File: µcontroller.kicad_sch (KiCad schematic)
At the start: 15 parts, among them U1 stm32G4

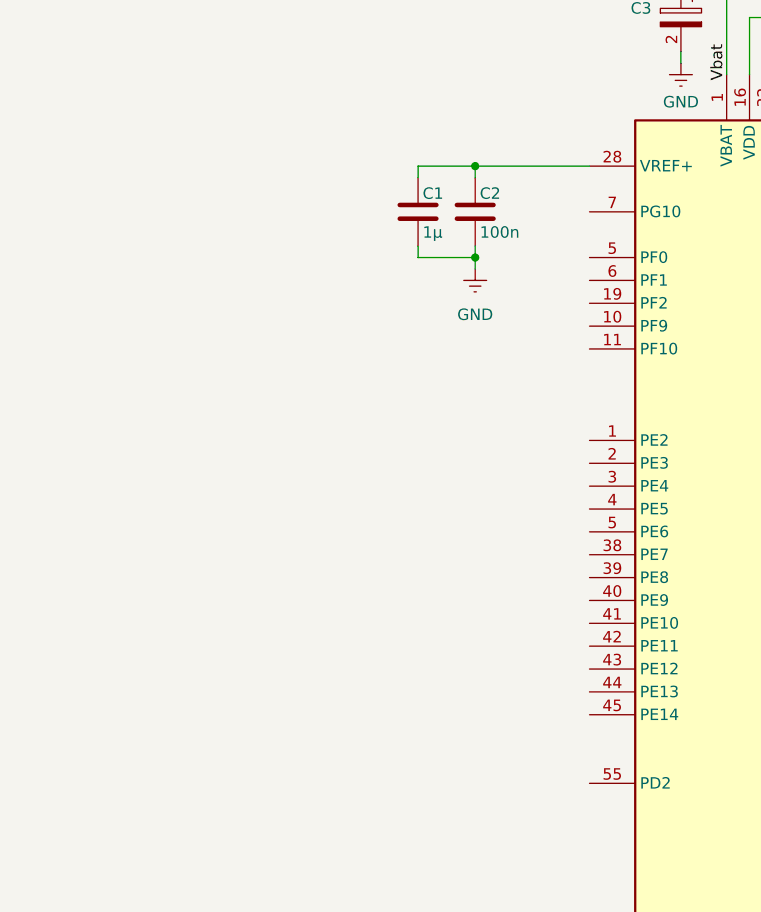
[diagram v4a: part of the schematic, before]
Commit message: pcb gesorteerd
al de main blokken bij elkaar gezet
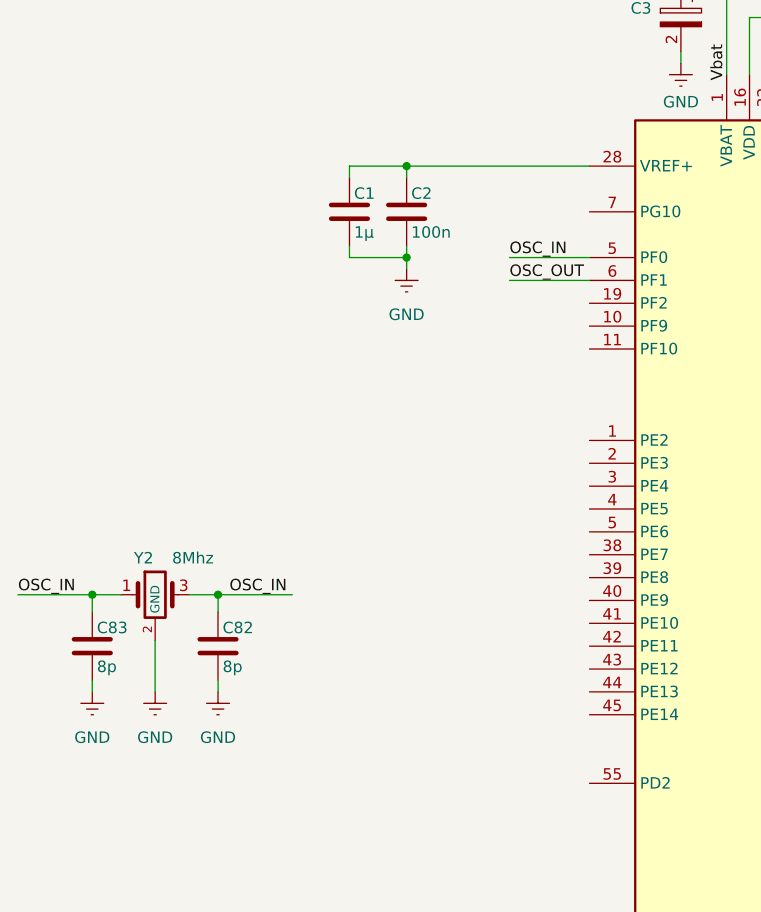
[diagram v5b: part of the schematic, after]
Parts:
- added C82, C83: 8p, Capacitor_SMD:C_0603_1608Metric, symbol Device:C
- added Y2: 8Mhz, Footprintsymbolen_samen:25Mhz crystal 8pF, symbol Schemasymbolen_samen:25Mhz_crystal
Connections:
- net GND: now also C82.2, C83.2, Y2.2 (GND)
- net OSC_IN: now reaches U1.5 (PE6)
- net OSC_IN: now also C82.1, C83.1, Y2.1, Y2.3
- net OSC_OUT: now reaches U1.6 (PF1)
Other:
- moved on the sheet: C1, C2

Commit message: al de main blokken bij elkaar gezet op juiste plaats
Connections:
- net GND: now also Y2.4 (GND)
- net OSC_IN: no longer C82.1, Y2.3
- net OSC_OUT: now also C82.1, Y2.3
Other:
- moved on the sheet: C82, C83, Y2
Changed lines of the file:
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@@
 	)
 	(junction
-		(at 67.945 99.695)
+		(at 68.58 100.33)
 		(diameter 0)
 		(color 0 0 0 0)
@@
 	)
 	(junction
-		(at 53.975 99.695)
+		(at 53.34 100.33)
 		(diameter 0)
 		(color 0 0 0 0)
@@
 	(wire
 		(pts
-			(xy 64.77 99.695) (xy 67.945 99.695)
+			(xy 64.77 100.33) (xy 77.47 100.33)
 		)
 		(stroke
@@
 	(wire
 		(pts
-			(xy 53.975 99.695) (xy 57.15 99.695)
-		)
-		(stroke
-			(width 0)
-			(type default)
-		)
-	)
-	(wire
-		(pts
 			(xy 154.94 85.09) (xy 158.75 85.09)
 		)
@@
 	(wire
 		(pts
-			(xy 53.975 99.695) (xy 53.975 101.6)
+			(xy 53.34 100.33) (xy 53.34 101.6)
 		)
 		(stroke
@@
 	(wire
 		(pts
+			(xy 60.96 105.41) (xy 60.96 110.49)
+		)
+		(stroke
+			(width 0)
+			(type default)
+		)
+	)
+	(wire
+		(pts
 			(xy 188.595 35.56) (xy 194.945 35.56)
 		)
@@
 	(wire
 		(pts
-			(xy 45.72 99.695) (xy 53.975 99.695)
+			(xy 45.72 100.33) (xy 57.15 100.33)
 		)
 		(stroke
@@
 	(wire
 		(pts
-			(xy 67.945 109.22) (xy 67.945 110.49)
+			(xy 68.58 109.22) (xy 68.58 110.49)
 		)
 		(stroke
@@
 	(wire
 		(pts
-			(xy 67.945 99.695) (xy 67.945 101.6)
+			(xy 68.58 100.33) (xy 68.58 101.6)
 		)
 		(stroke
@@
 	(wire
 		(pts
-			(xy 53.975 109.22) (xy 53.975 110.49)
+			(xy 53.34 109.22) (xy 53.34 110.49)
 		)
 		(stroke
@@
 	(wire
 		(pts
-			(xy 60.96 104.775) (xy 60.96 110.49)
-		)
-		(stroke
-			(width 0)
-			(type default)
-		)
-	)
-	(wire
-		(pts
 			(xy 134.62 186.69) (xy 134.62 189.23)
 		)
@@
 	(wire
 		(pts
-			(xy 67.945 99.695) (xy 76.2 99.695)
-		)
-		(stroke
-			(width 0)
-			(type default)
-		)
-	)
-	(wire
-		(pts
 			(xy 127 35.56) (xy 129.54 35.56)
 		)
@@
 		)
 	)
-	(label "OSC_IN"
-		(at 69.215 99.695 0)
+	(label "OSC_OUT"
+		(at 69.215 100.33 0)
 		(effects
 			(font
@@
 	)
 	(label "OSC_IN"
-		(at 45.72 99.695 0)
+		(at 45.72 100.33 0)
 		(effects
 			(font
@@
 	(symbol
 		(lib_id "Device:C")
-		(at 67.945 105.41 0)
+		(at 68.58 105.41 0)
 		(unit 1)
 		(body_style 1)
@@
 		(dnp no)
 		(property "Reference" "C82"
-			(at 68.453 103.378 0)
+			(at 69.088 103.378 0)
 			(show_name no)
 			(do_not_autoplace no)
@@
 		)
 		(property "Value" "8p"
-			(at 68.453 107.696 0)
+			(at 69.088 107.696 0)
 			(show_name no)
 			(do_not_autoplace no)
@@
 		)
 		(property "Footprint" "Capacitor_SMD:C_0603_1608Metric"
-			(at 68.9102 109.22 0)
+			(at 69.5452 109.22 0)
 			(hide yes)
 			(show_name no)
@@
 		)
 		(property "Datasheet" ""
-			(at 67.945 105.41 0)
+			(at 68.58 105.41 0)
 			(hide yes)
 			(show_name no)
@@
 		)
 		(property "Description" "Unpolarized capacitor"
-			(at 67.945 105.41 0)
+			(at 68.58 105.41 0)
 			(hide yes)
 			(show_name no)
@@
 	(symbol
 		(lib_id "Device:C")
-		(at 53.975 105.41 0)
+		(at 53.34 105.41 0)
 		(unit 1)
 		(body_style 1)
@@
 		(dnp no)
 		(property "Reference" "C83"
-			(at 54.483 103.378 0)
+			(at 53.848 103.378 0)
 			(show_name no)
 			(do_not_autoplace no)
@@
 		)
 		(property "Value" "8p"
-			(at 54.483 107.696 0)
+			(at 53.848 107.696 0)
 			(show_name no)
 			(do_not_autoplace no)
@@
 		)
 		(property "Footprint" "Capacitor_SMD:C_0603_1608Metric"
-			(at 54.9402 109.22 0)
+			(at 54.3052 109.22 0)
 			(hide yes)
 			(show_name no)
@@
 		)
 		(property "Datasheet" ""
-			(at 53.975 105.41 0)
+			(at 53.34 105.41 0)
 			(hide yes)
 			(show_name no)
@@
 		)
 		(property "Description" "Unpolarized capacitor"
-			(at 53.975 105.41 0)
+			(at 53.34 105.41 0)
 			(hide yes)
 			(show_name no)
@@
 	(symbol
 		(lib_id "Schemasymbolen_samen:25Mhz_crystal")
-		(at 57.15 98.425 0)
+		(at 57.15 99.06 0)
 		(unit 1)
 		(body_style 1)
@@
 		(dnp no)
 		(property "Reference" "Y2"
-			(at 59.69 95.631 0)
+			(at 59.69 96.266 0)
 			(show_name no)
 			(do_not_autoplace no)
@@
 		)
 		(property "Value" "8Mhz"
-			(at 65.151 95.631 0)
+			(at 65.151 96.266 0)
 			(show_name no)
 			(do_not_autoplace no)
@@
 		)
 		(property "Footprint" "Footprintsymbolen_samen:25Mhz crystal 8pF"
-			(at 52.578 88.011 0)
+			(at 52.578 88.646 0)
 			(hide yes)
 			(show_name no)
@@
 		)
 		(property "Datasheet" "https://www.mouser.be/datasheet/3/1460/1/LFXTAL085880.pdf"
-			(at 73.152 92.837 0)
+			(at 73.152 93.472 0)
 			(hide yes)
 			(show_name no)
@@
 		)
 		(property "Description" "LFXTAL085880"
-			(at 57.15 98.425 0)
+			(at 48.768 95.504 0)
 			(hide yes)
 			(show_name no)
@@
 	(symbol
 		(lib_id "power:GNDREF")
-		(at 53.975 110.49 0)
+		(at 53.34 110.49 0)
 		(unit 1)
 		(body_style 1)
@@
 		(fields_autoplaced yes)
 		(property "Reference" "#PWR0103"
-			(at 53.975 116.84 0)
+			(at 53.34 116.84 0)
 			(hide yes)
 			(show_name no)
@@
 		)
 		(property "Value" "GND"
-			(at 53.975 115.57 0)
+			(at 53.34 115.57 0)
 			(show_name no)
 			(do_not_autoplace no)
@@
 		)
 		(property "Footprint" ""
-			(at 53.975 110.49 0)
+			(at 53.34 110.49 0)
 			(hide yes)
 			(show_name no)
@@
 		)
 		(property "Datasheet" ""
-			(at 53.975 110.49 0)
+			(at 53.34 110.49 0)
 			(hide yes)
 			(show_name no)
@@
 		)
 		(property "Description" "Power symbol creates a global label with name \"GNDREF\" , reference supply ground"
-			(at 53.975 110.49 0)
+			(at 53.34 110.49 0)
 			(hide yes)
 			(show_name no)
@@
 	(symbol
 		(lib_id "power:GNDREF")
-		(at 67.945 110.49 0)
+		(at 68.58 110.49 0)
 		(unit 1)
 		(body_style 1)
@@
 		(fields_autoplaced yes)
 		(property "Reference" "#PWR0102"
-			(at 67.945 116.84 0)
+			(at 68.58 116.84 0)
 			(hide yes)
 			(show_name no)
@@
 		)
 		(property "Value" "GND"
-			(at 67.945 115.57 0)
+			(at 68.58 115.57 0)
 			(show_name no)
 			(do_not_autoplace no)
@@
 		)
 		(property "Footprint" ""
-			(at 67.945 110.49 0)
+			(at 68.58 110.49 0)
 			(hide yes)
 			(show_name no)
@@
 		)
 		(property "Datasheet" ""
-			(at 67.945 110.49 0)
+			(at 68.58 110.49 0)
 			(hide yes)
 			(show_name no)
@@
 		)
 		(property "Description" "Power symbol creates a global label with name \"GNDREF\" , reference supply ground"
-			(at 67.945 110.49 0)
+			(at 68.58 110.49 0)
 			(hide yes)
 			(show_name no)

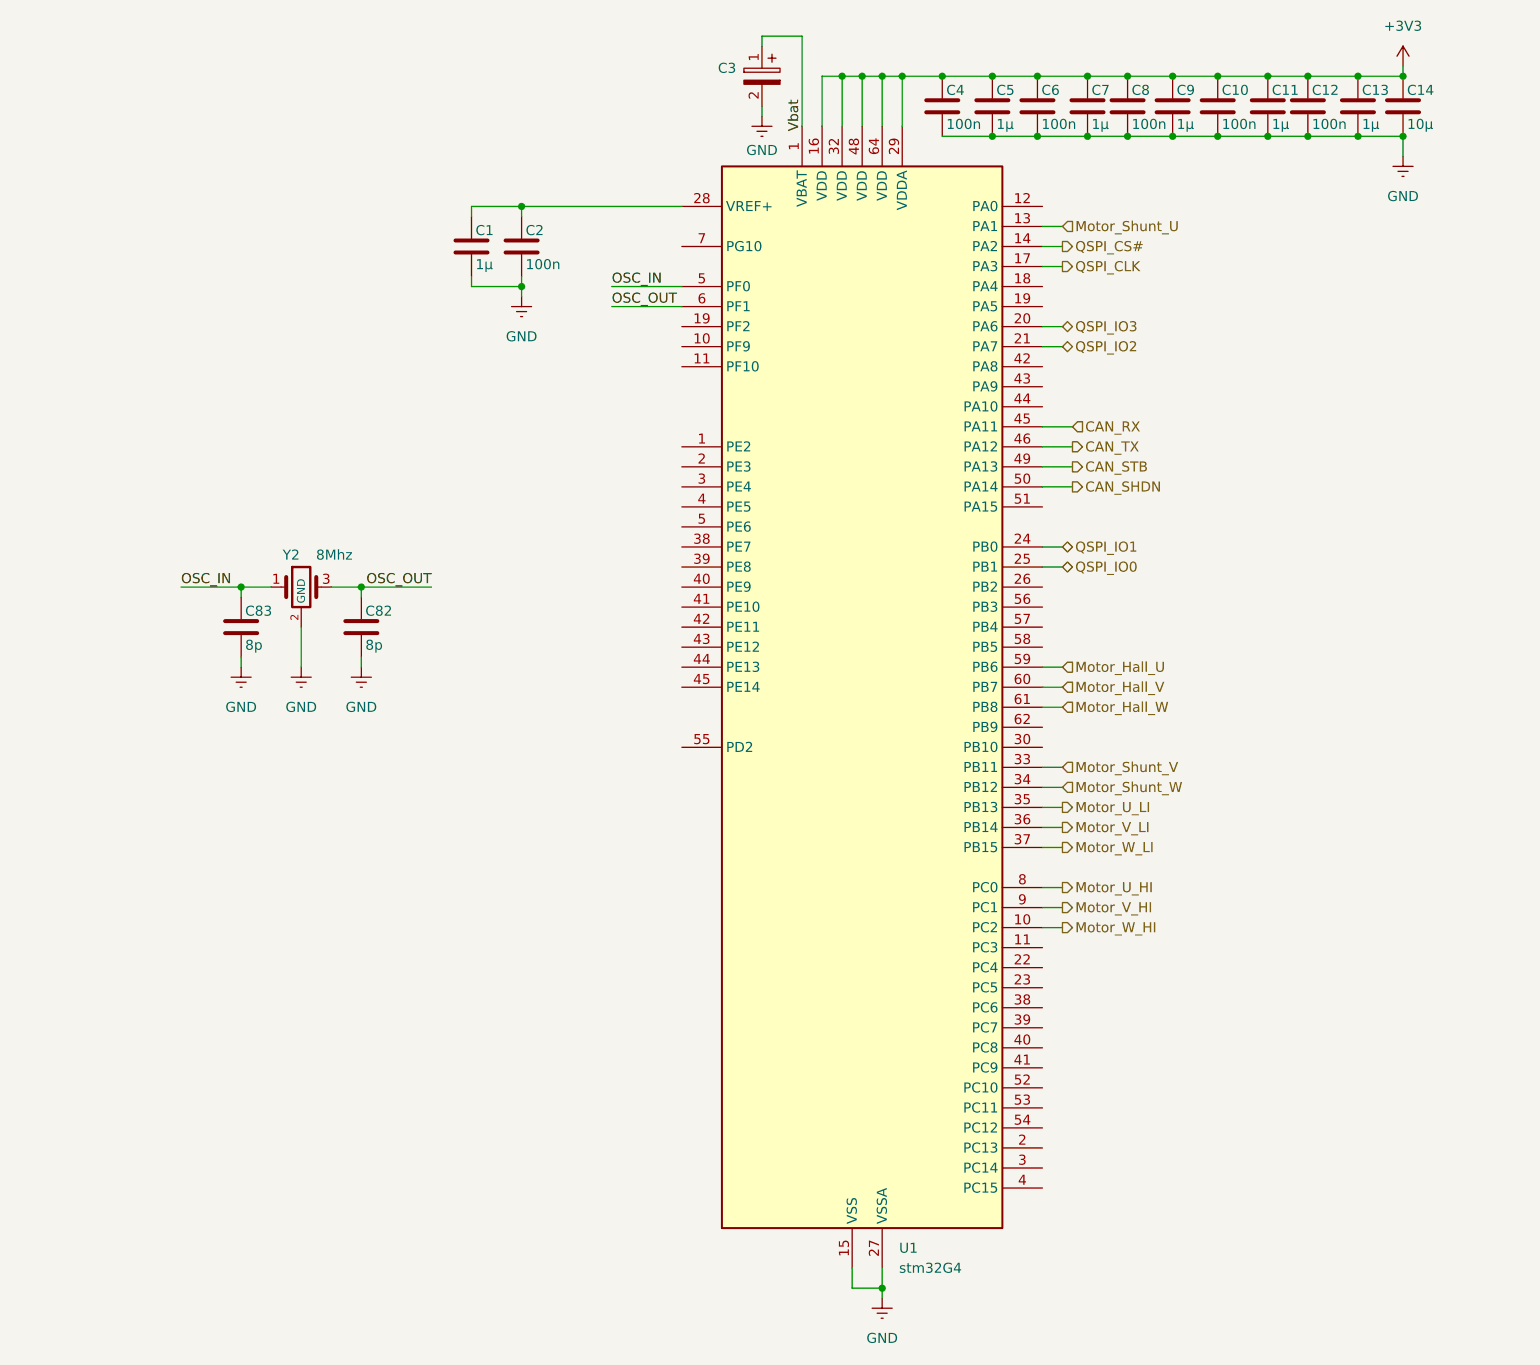
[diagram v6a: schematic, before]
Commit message: connector
connector toegevoegd en wat pinnen aangepast
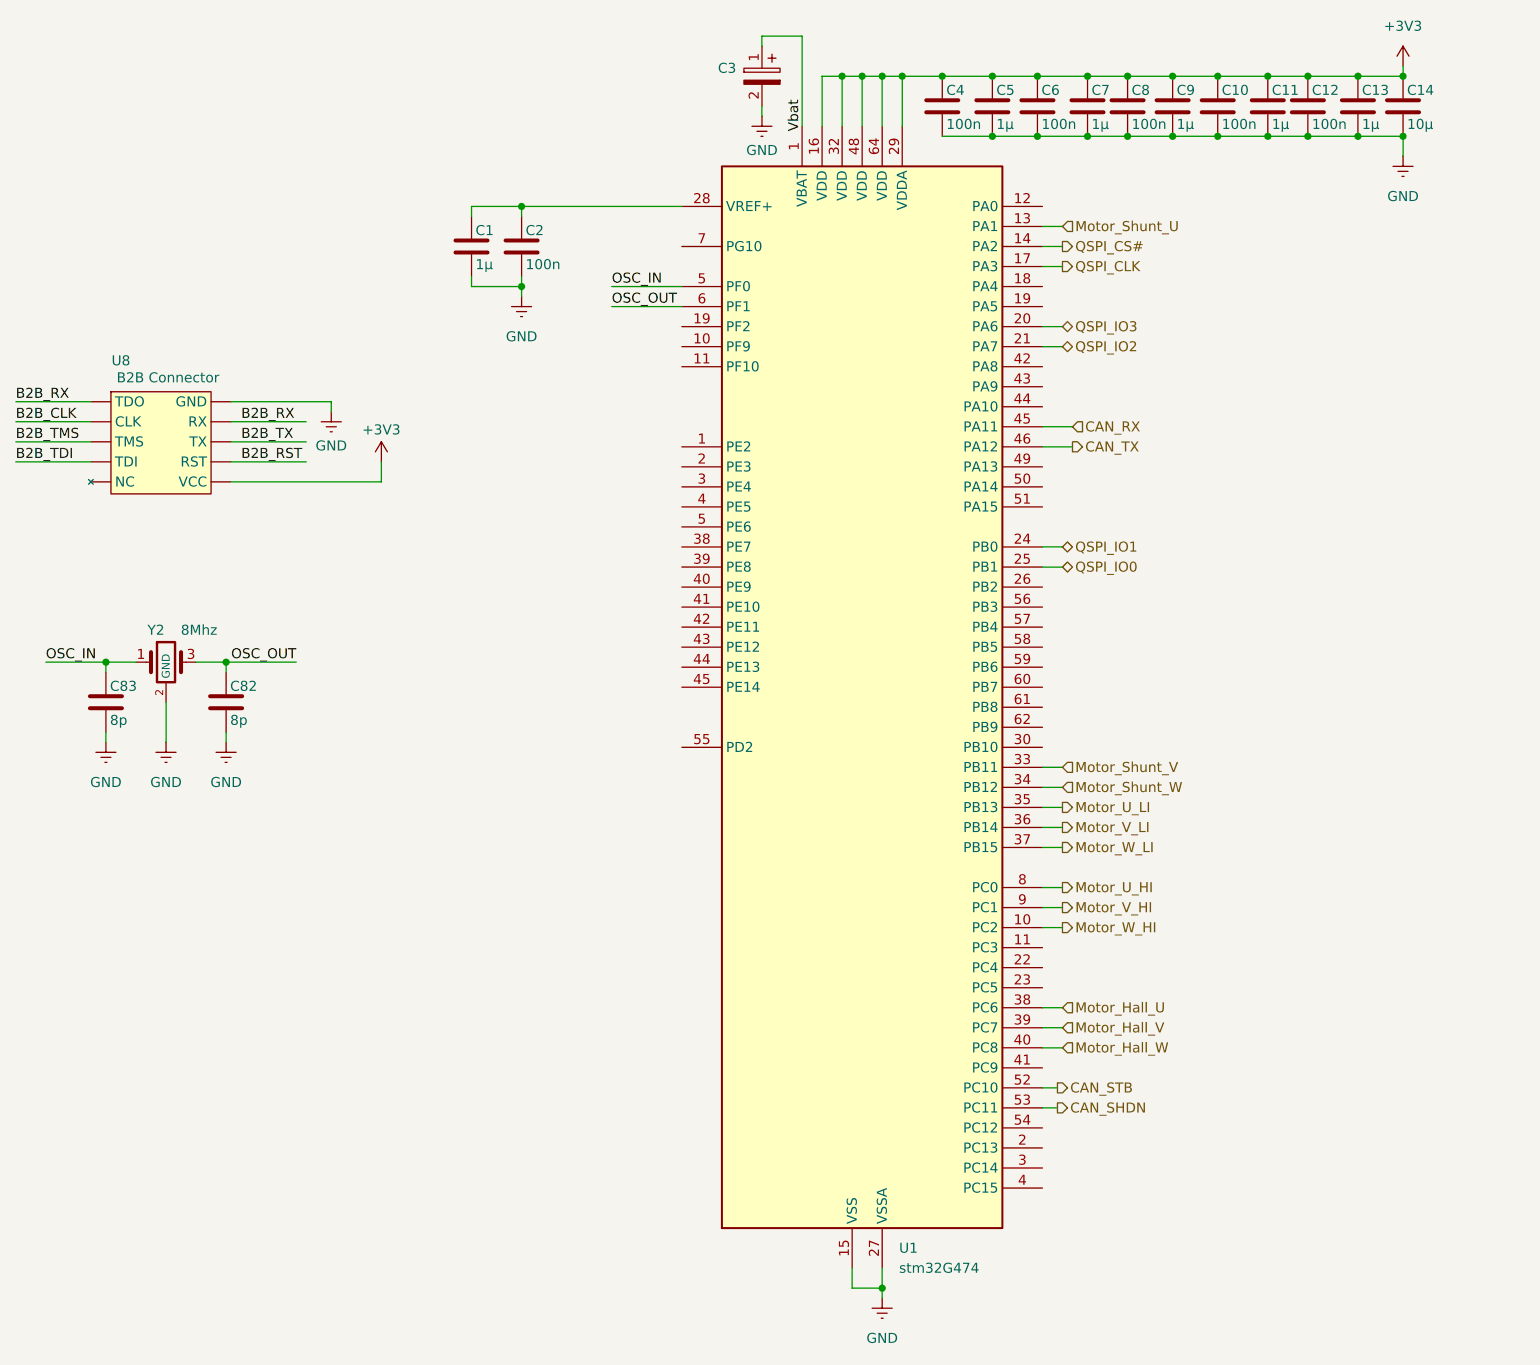
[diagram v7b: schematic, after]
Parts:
- added U8: B2B Connector, symbol Symbolen_samen:B2B_Connector
- U1: value stm32G4 -> stm32G474
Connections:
- net +3V3: now also U8. (VCC)
- net CAN_SHDN: now also U1.53 (PC11); no longer U1.50 (PA14)
- net CAN_STB: now also U1.52 (PC10); no longer U1.49 (PA13)
- net GND: now also U8. (VCC)
- net Motor_Hall_U: now also U1.38 (PC6); no longer U1.59 (PB6)
- net Motor_Hall_V: now also U1.39 (PC7); no longer U1.60 (PB7)
- net Motor_Hall_W: now also U1.40 (PC8); no longer U1.61 (PB8)
- new net B2B_CLK: U8. (VCC)
- new net B2B_RST: U8. (VCC)
- new net B2B_RX: U8. (VCC)
- new net B2B_TDI: U8. (VCC)
- new net B2B_TMS: U8. (VCC)
- new net B2B_TX: U8. (VCC)
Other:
- moved on the sheet: C82, C83, Y2

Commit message: schema's finalized
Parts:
- added C41: 100n, Capacitor_SMD:C_0603_1608Metric, symbol Device:C
- added R32: 47k, Resistor_SMD:R_0603_1608Metric, symbol Device:R
- added R33: 2.7k, Resistor_SMD:R_0603_1608Metric, symbol Device:R
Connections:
- net B2B_TDI is gone; now on net GND: U8. (VCC)
- net B2B_CLK: now also U1.50 (PA14)
- net B2B_RST: now also U1.7 (PG10), C41.1
- net B2B_RX: now also U1.23 (PC5)
- net B2B_TMS: now also U1.49 (PA13)
- net B2B_TX: now also U1.22 (PC4)
- net GND: now also C41.2, R33.1
- net at U1.12 (PA0): now also R32.1, R33.2
- net Ethercat_IRQ: now reaches U1.42 (PA8)
- net Ethercat_Sync0: now reaches U1.43 (PA9)
- net Ethercat_Sync1: now reaches U1.44 (PA10)
- net B2B_TDO: now reaches U1.56 (PB3)
- net B2B_TDO: now also U8. (VCC)
- new net +48V: R32.2
- no-connect marks 0 -> 1
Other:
- note added: "Spanningsdeler voor ADC om overspanning te detecteren"
- moved on the sheet: C1, C2
